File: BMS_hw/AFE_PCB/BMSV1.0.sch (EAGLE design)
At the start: 238 parts, among them IC1 MC33771BEP, IC2 SFH6156, IC3 MIC28515V1, IC4 FOD8384-COC, IC5 FOD8384-COC, IC6 FOD8384-COC, J2 NTC, Q1 IRLML5203, Q2 IRLML5203, T1 IPT020N10N3V1, T2 IPT020N10N3V1, T3 IPT020N10N3V1, T4 IPT020N10N3V1, X1 87758-2016, X2 87758-1816, X3 22-23-2041, X4 87758-2016, X5 22-23-2051

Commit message: board layout itt@1
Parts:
- removed C79, C81, C85, C87, C91: 0.047uF, ipc-7351-capacitor:CAPACITOR_0402
- removed C80, C82, C86, C88, C92: 0.47uF, ipc-7351-capacitor:CAPACITOR_0402
- removed R105: 10k, ipc-7351-resistor:RESISTOR_0402
- added C39: 0.47uF, ipc-7351-capacitor:CAPACITOR_1206
- added C40, C41: 0.047uF, ipc-7351-capacitor:CAPACITOR_0402
- added C61: 0.22uF, ipc-7351-capacitor:CAPACITOR_0402
- added C63: (no value), ipc-7351-capacitor:POLARISED_CASE_E
- added C64, C70: 47nF, ipc-7351-capacitor:CAPACITOR_1210
- added C65, C68: 47nF, ipc-7351-capacitor:CAPACITOR_0402
- added C69: 47nF, ipc-7351-capacitor:CAPACITOR_0603
- added R68, R69: 10k, ipc-7351-resistor:RESISTOR_0402
- added TP1: TPTH7035, simpa:TPTH7035
- C1: value 0.22uF -> 0.047uF; device ipc-7351-capacitor:CAPACITOR_0402 -> ipc-7351-capacitor:CAPACITOR_0603
- C10, C11, C12, C32, C33, C34, C35, C36, C37, C8: value 0.047uF -> 0.47uF; device ipc-7351-capacitor:CAPACITOR_0402 -> ipc-7351-capacitor:CAPACITOR_1206
- C13, C9: value 47nF -> 0.47uF; device ipc-7351-capacitor:CAPACITOR_0402 -> ipc-7351-capacitor:CAPACITOR_1206
- C14: value 2.2uF -> 0.47uF; device ipc-7351-capacitor:CAPACITOR_0402 -> ipc-7351-capacitor:CAPACITOR_1206
- C15: value 2.2uF -> 0.047uF
- C16: value 1uF -> 0.047uF
- C17: value 47nF -> 0.047uF
- C18, C19, C20, C21: value 0.47uF -> 0.047uF
- C2, C24, C26, C5: value 47nF -> 0.047uF; device ipc-7351-capacitor:CAPACITOR_0402 -> ipc-7351-capacitor:CAPACITOR_0603
- C22: value 47nF -> 2.2uF; device ipc-7351-capacitor:CAPACITOR_0603 -> ipc-7351-capacitor:CAPACITOR_0402
- C23: value 47nF -> .047uF; device ipc-7351-capacitor:CAPACITOR_1210 -> ipc-7351-capacitor:CAPACITOR_0402
- C25: value 47nF -> 0.047uF; device ipc-7351-capacitor:CAPACITOR_1210 -> ipc-7351-capacitor:CAPACITOR_0603
- C27, C28, C29: value 0.47uF -> 0.047uF; device ipc-7351-capacitor:CAPACITOR_0402 -> ipc-7351-capacitor:CAPACITOR_0603
- C3, C31, C4, C7: device ipc-7351-capacitor:CAPACITOR_0402 -> ipc-7351-capacitor:CAPACITOR_0603
- C30: value (none) -> 0.047uF; device ipc-7351-capacitor:CAPACITOR_0402 -> ipc-7351-capacitor:CAPACITOR_0603
- C38: value (none) -> 0.47uF; device ipc-7351-capacitor:POLARISED_CASE_E -> ipc-7351-capacitor:CAPACITOR_1206
- C6: value 6.8uF -> 0.047uF; device ipc-7351-capacitor:CAPACITOR_0402 -> ipc-7351-capacitor:CAPACITOR_0603
- C66: value .047uF -> 47nF
- C67: value 2.2uF -> 47nF
- C71: value 0.047uF -> 47nF
- C72, C74: value 0.47uF -> 47nF
- C73: value 0.047uF -> 1uF
- C75: value 0.047uF -> 6.8uF
- C76: value 0.47uF -> 2.2uF
- C77: value 0.047uF -> 2.2uF
- C78: value 0.047uF -> (none)
- D1: device ipc-7351-diode:ZENER_SOD-123 -> ipc-7351-diode:SCHOTTKY_SOD-123
- D10: value 8.2v -> (none); device ipc-7351-diode:SCHOTTKY_SOD-123 -> ipc-7351-diode:DIODE_SOD-123
- D11: value 20v -> 8.2v; device ipc-7351-diode:SCHOTTKY_SOD-123 -> ipc-7351-diode:ZENER_SOD-123
- D12: value 27v -> (none)
- D13: value 43v -> (none)
- D14: value 75v -> (none)
- D15: value 2v -> (none)
- D16: value 2v -> (none); device ipc-7351-diode:SCHOTTKY_SOD-123 -> ipc-7351-diode:ZENER_SOD-123
- D17, D18: value 2v -> SFH48225; device ipc-7351-diode:SCHOTTKY_SOD-123 -> GreenFuel:SFH48225
- D19: value (none) -> SFH48225; device ipc-7351-diode:SCHOTTKY_SOD-123 -> GreenFuel:SFH48225
- D2: value (none) -> 20v; device ipc-7351-diode:DIODE_SOD-123 -> ipc-7351-diode:SCHOTTKY_SOD-123
- D3: value SFH48225 -> 27v; device GreenFuel:SFH48225 -> ipc-7351-diode:SCHOTTKY_SOD-123
- D4: value SFH48225 -> 43v; device GreenFuel:SFH48225 -> ipc-7351-diode:SCHOTTKY_SOD-123
- D5: value SFH48225 -> 75v; device GreenFuel:SFH48225 -> ipc-7351-diode:SCHOTTKY_SOD-123
- D6: value (none) -> 2v; device ipc-7351-diode:ZENER_SOD-123 -> ipc-7351-diode:SCHOTTKY_SOD-123
- D7, D8, D9: value (none) -> 2v
- JP1: device GreenFuel:PINOLED-4 -> adafruit:PINHD-1X1CB
- JP3: device adafruit:PINHD-1X1CB -> GreenFuel:PINOLED-4
- R1: value 10 -> (none)
- R10, R9: value 180E -> (none)
- R11: value 2E2 -> 180E; device ipc-7351-resistor:RESISTOR_0402 -> ipc-7351-resistor:RESISTOR_1210
- R12: value 200k -> 180E; device ipc-7351-resistor:RESISTOR_0402 -> ipc-7351-resistor:RESISTOR_1210
- R13: value 180E -> 39E; device ipc-7351-resistor:RESISTOR_0402 -> ipc-7351-resistor:RESISTOR_1210
- R14, R6: device ipc-7351-resistor:RESISTOR_0402 -> ipc-7351-resistor:RESISTOR_1210
- R15: value 100k -> 3k
- R16, R21: value 127E -> 3k
- R2, R4: value 100 -> (none)
- R22, R23, R24, R25: value 127E -> 2k
- R26, R27, R28: value 3k -> 2k
- R3: value 127E -> (none)
- R31, R70, R72, R74, R78: value 2k -> 10k
- R32, R33, R36, R37: value 2k -> (none)
- R34: value 2k -> 0R
- R35: value 2k -> 100; device ipc-7351-resistor:RESISTOR_0402 -> ipc-7351-resistor:RESISTOR_1210
- R38, R41, R42, R8: value 10k -> (none)
- R39, R7: value LRMAP3920SUNT -> 100; device GreenFuel:LRMAP3920SUNT -> ipc-7351-resistor:RESISTOR_1210
- R40: value 10k -> 100; device ipc-7351-resistor:RESISTOR_0402 -> ipc-7351-resistor:RESISTOR_1210
- R44, R45, R50, R51, R52, R53, R54, R55: value (none) -> 3k
- R46: value 3k -> 180E; device ipc-7351-resistor:RESISTOR_0402 -> ipc-7351-resistor:RESISTOR_1210
- R47, R48, R49: value (none) -> 180E; device ipc-7351-resistor:RESISTOR_0402 -> ipc-7351-resistor:RESISTOR_1210
- R5: value 127E -> 100; device ipc-7351-resistor:RESISTOR_0402 -> ipc-7351-resistor:RESISTOR_1210
- R56, R57, R58: value (none) -> 2k
- R59, R60, R61, R62, R63: value 10k -> 2k
- R66: value 10k -> 10
- R71, R73, R77: value 3k -> 10k
- R75: value 100 -> 10k
- R76: value 180E -> 10k
- R79, R83, R85: value 3k -> 127E
- R80, R86: value 2k -> 127E
- R81: value 100 -> LRMAP3920SUNT; device ipc-7351-resistor:RESISTOR_0402 -> GreenFuel:LRMAP3920SUNT
- R82, R88: value 180E -> 127E
- R84: value 2k -> LRMAP3920SUNT; device ipc-7351-resistor:RESISTOR_0402 -> GreenFuel:LRMAP3920SUNT
- R87: value 100 -> 127E
- R89: value 180E -> 100k
- R90: value 2k -> 200k
- R91: value 3k -> 2E2
- X1: value 87758-2016 -> 87758-1816; device con-molex:87758-2016 -> con-molex:87758-1816
- X2: value 87758-1816 -> 87758-2016; device con-molex:87758-1816 -> con-molex:87758-2016
- X3: value 22-23-2041 -> 87758-2016; device GreenFuel:22-23-2041 -> con-molex:87758-2016
- X4: value 87758-2016 -> 22-23-2051; device con-molex:87758-2016 -> GreenFuel:22-23-2051
- X5: value 22-23-2051 -> 22-23-2041; device GreenFuel:22-23-2051 -> GreenFuel:22-23-2041
- renumbered C100 to C62, C101 to C60, C102 to C48, C103 to C49, C104 to C50, C105 to C52, C106 to C53, C107 to C51, C108 to C54, C83 to C43, C84 to C42, C89 to C45, C90 to C44, C93 to C46, C94 to C47, C95 to C59, C96 to C55, C97 to C56, C98 to C57, C99 to C58, J2 to J1
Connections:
- removed net 15V_AUX: IC4.VDD, IC5.VDD, IC6.VDD, X4-17.S
- removed net C_FET: X4-9.S
- removed net D_FET: X4-19.S
- removed net N$26: C66.1, IC1.VANA
- removed net N$42: C74.1, R71.2, R72.1
- removed net N$44: C80.1, R77.2, R78.1
- removed net N$45: C82.1, R79.2, R80.1
- removed net N$47: C88.1, R85.2, R86.1
- removed net N$63: CELL1-.S, R53.1
- removed net VBATT-: R42.1
- removed net VCC: C22.1, C23.1, L1.2, R22.1
- new net +15V: C69.1, C70.1, IC4.VDD, IC5.VDD, IC6.VDD, L1.2, R85.1, X2-17.S
- new net BGND: CELL1-.S, R34.1, R38.1, R81.4, R84.4
- new net GATE: D10.K, D11.K, R93.1, R94.2, T3.G, T4.G
- new net N$10: C38.1, R54.2, R62.1
- new net N$16: C37.1, R53.2, R60.1
- new net N$23: C36.1, R52.2, R59.1
- new net PCHG_GATE: IC6.ANODE, X2-4.S
- new net VANA: C23.1, IC1.VANA
- net !MCLR: now also X2-10.S, X4-5.S; no longer X4-10.S, X5-5.S
- net 3.3V: now also JP3.3, R101.2, X2-12.S, X3-16.S, X4-4.S; no longer JP1.3, R59.2, X1-16.S, X4-12.S, X5-4.S
- net AGND: now also X1-1.S; no longer X2-1.S
- net BST: now also C65.1; no longer C24.1
- net CANH: now also D15.K, X5-4.S; no longer D19.K, X3-4.S
- net CANL: now also D14.K, X5-3.S; no longer D9.K, X3-3.S
- net CB_1: now also R49.2; no longer R89.2
- net CB_10/9_C: now also C7.1, D2.A, R10.1, R17.1; no longer C12.1, D11.A, R19.1, R58.1
- net CB_11: now also R6.2; no longer R4.2
- net CB_12: now also D4.A, R11.2; no longer D13.A, R9.2
- net CB_12/11_C: now also C6.1, R16.1, R9.2; no longer C11.1, R18.1, R56.2
- net CB_13: now also R7.2; no longer R6.2
- net CB_13/12_C: now also C1.1, R1.2, R11.1, R20.1, R7.1; no longer C3.1, R27.1, R44.2, R6.1, R9.1
- net CB_13/12_C1: now also C4.1, R21.1, R4.2, R6.1; no longer C8.1, R28.1, R4.1, R45.2
- net CB_13/12_C2: now also C2.1, R12.1, R18.1, R2.2, R5.1; no longer C4.1, R10.1, R2.1, R20.1, R47.2
- net CB_13/12_C6: now also C26.1, R36.2, R39.1, R46.1, R51.1; no longer C73.1, R49.2, R71.1, R75.1, R76.1
- net CB_13/12_C7: now also C24.1, R32.2, R35.1, R47.1, R52.1; no longer C79.1, R51.2, R77.1, R81.1, R82.1
- net CB_13/12_C8: now also C28.1, R37.2, R40.1, R48.1, R55.1; no longer C85.1, R52.2, R83.1, R87.1, R88.1
- net CB_14: now also D3.A; no longer D12.A
- net CB_14/13_C: now also C5.1, R15.1, R8.2; no longer C10.1, R17.1, R57.2
- net CB_2: now also R48.2; no longer R88.2
- net CB_2/1_C: now also C31.1, R41.2, R54.1; no longer C87.1, R55.2, R85.1
- net CB_3: now also R40.2; no longer R87.2
- net CB_4: now also R47.2; no longer R82.2
- net CB_4/3_C: now also C30.1, R43.2, R53.1; no longer C81.1, R54.2, R79.1
- net CB_5: now also R35.2; no longer R81.2
- net CB_6: now also R46.2; no longer R76.2
- net CB_6/5_C: now also C25.1, R33.2, R44.1; no longer C75.1, R50.2, R73.1
- net CB_7: now also R39.2; no longer R75.2
- net CB_8: now also R12.2; no longer R10.2
- net CB_8/7_C: now also C29.1, D1.A, R42.2, R50.1; no longer C71.1, D10.A, R46.1, R48.2
- net CB_9: now also R5.2; no longer R2.2
- net CELL1-: now also C27.1, R38.2, R45.1, R49.1, R98.1; no longer C91.1, R53.2, R89.1, R91.1
- net CELL14+: now also C3.1, R19.1, R3.2, R66.1; no longer C7.1, R1.1, R26.1, R43.2
- net CHG_FET: now also IC5.VO, Q1.S; no longer IC4.ANODE
- net CHG_GATE: now also IC5.ANODE, X2-9.S; no longer D1.K, D2.K, IC6.VO, Q1.S, R30.2, R38.1, T1.G, T2.G
- net CT_1: now also R62.2; no longer R86.2
- net CT_10: now also C18.2, C19.1, R26.2; no longer C34.2, C35.1, R35.2
- net CT_11: now also C17.2, C18.1, R25.2; no longer C33.2, C34.1, R34.2
- net CT_12: now also C16.2, C17.1, R24.2; no longer C32.2, C33.1, R33.2
- net CT_13: now also C15.2, C16.1, R23.2; no longer C31.2, C32.1, R32.2
- net CT_14: now also C15.1, R22.2; no longer C31.1, R31.2
- net CT_2: now also R61.2; no longer R84.2
- net CT_3: now also R60.2; no longer R80.2
- net CT_4: now also R59.2; no longer R78.2
- net CT_5: now also C41.2, R58.2; no longer C77.2, R74.2
- net CT_6: now also C40.2, C41.1, R57.2; no longer C77.1, C78.2, R72.2
- net CT_7: now also C21.2, C40.1, R56.2; no longer C37.2, C78.1, R70.2
- net CT_8: now also C20.2, C21.1, R28.2; no longer C36.2, C37.1, R37.2
- net CT_9: now also C19.2, C20.1, R27.2; no longer C35.2, C36.1, R36.2
- net CT_REF: now also R63.2; no longer R90.2
- net C_HIGH(VC14): now also X1-18.S; no longer X2-18.S
- net DSG_FET: now also IC4.VO, R92.2, T1.G, T2.G; no longer IC6.ANODE
- net DSG_GATE: now also IC4.ANODE, X2-19.S; no longer IC4.VO, R29.2, T3.G, T4.G
- net FAULT: now also X2-5.S; no longer X4-5.S
- net FB: now also C66.2, R85.2, R86.1; no longer C17.2, R22.2, R23.1
- net GND: now also C24.2, C30.2, C31.2, C32.2, C33.2, C34.2, C35.2, C36.2, C37.2, C38.2, C39.2, C6.2, C61.2, C63.-, C64.2, C68.2, C69.2, C70.2, C77.2, C78.1, D15.A, D16.A, D5.A, D7.K, D9.K, JP3.4, R100.2, R102.2, R103.2, R104.2, R30.2, R34.2, R86.2, R89.2, R95.2, R96.2, R97.2, X1-11.S, X2-1.S, X2-15.S, X2-18.S, X2-2.S, X2-20.S, X2-3.S, X2-6.S, X2-7.S, X2-8.S, X3-1.S, X3-10.S, X3-14.S, X3-18.S, X3-2.S, X3-20.S, X3-3.S, X3-7.S, X3-8.S; no longer C15.2, C16.2, C18.2, C19.2, C20.2, C21.2, C30.1, C38.-, C66.2, C75.2, C79.2, C80.2, C81.2, C82.2, C85.2, C86.2, C87.2, C88.2, C91.2, C92.2, D16.K, D18.K, D19.A, D6.A, D9.A, JP1.4, R15.2, R23.2, R39.4, R40.2, R41.2, R60.2, R61.2, R62.2, R65.2, R67.2, R7.4, R8.2, X1-1.S, X1-10.S, X1-14.S, X1-18.S, X1-2.S, X1-20.S, X1-3.S, X1-7.S, X1-8.S, X2-11.S, X4-15.S, X4-18.S, X4-2.S, X4-20.S, X4-3.S, X4-6.S, X4-7.S, X4-8.S, X5-1.S
- net GPIO0: now also R72.1; no longer R99.1
- net GPIO1: now also R73.1; no longer R100.1
- net GPIO2: now also R74.1; no longer R101.1
- net GPIO3: now also R75.1; no longer R102.1
- net GPIO4: now also R76.1; no longer R103.1
- net GPIO5: now also R77.1; no longer R104.1
- net GPIO6: now also R78.1; no longer R105.1
- net ILIM: now also R80.1, R82.1; no longer R16.1, R24.1
- net INTL_IN2: now also D12.A, X5-1.S; no longer D7.A, X3-1.S
- net INTL_OUT1: now also JP2.1, X5-2.S; no longer JP3.1, X3-2.S
- net ISENSE+: now also C71.1, C75.1, R87.2; no longer C13.1, C6.1, R5.2
- net ISENSE-: now also C72.1, C75.2, R88.2; no longer C2.1, C6.2, R3.2
- net ISP: now also X2-11.S; no longer X4-11.S
- net KEY-IN: now also D12.K, D13.K, R99.1; no longer D7.K, D8.K, R63.1
- net N$1: now also C12.1, R19.2, R22.1; no longer C27.1, R26.2, R31.1
- net N$11: now also D6.A, D7.A; no longer D17.A, D18.A
- net N$17: now also R89.1, R90.1; no longer R12.1, R15.1
- net N$18: now also C73.1; no longer C16.1
- net N$19: now also D10.A, R93.2; no longer D2.A, R38.2
- net N$2: now also C11.1, R18.2, R28.1; no longer C21.1, R20.2, R37.1
- net N$20: now also IC5.CATHODE, R96.1; no longer IC4.CATHODE, R8.1
- net N$21: now also C74.1, R79.2; no longer C26.1, R25.2
- net N$24: now also C66.1, R83.2; no longer C17.1, R21.2
- net N$25: now also IC4.CATHODE, R95.1; no longer IC6.CATHODE, R40.1
- net N$27: now also IC6.CATHODE, R97.1; no longer IC5.CATHODE, R41.1
- net N$28: now also R98.2; no longer R42.2
- net N$29: now also C63.+, C64.1, R3.1, R79.1; no longer C25.1, C38.+, R25.1, R43.1
- net N$3: now also D8.A, D9.A; no longer D15.A, D16.A
- net N$30: now also R31.1; no longer R64.1
- net N$31: now also R31.2; no longer R64.2
- net N$33: now also R36.1; no longer R49.1
- net N$34: now also R29.1; no longer R66.1
- net N$35: now also R33.1; no longer R50.1
- net N$37: now also R1.1; no longer R44.1
- net N$38: now also C35.1, R51.2, R57.1; no longer IC5.VO
- net N$39: now also R4.1; no longer R45.1
- net N$4: now also C14.1, R21.2, R26.1; no longer C29.1, R28.2, R35.1
- net N$40: now also R2.1; no longer R47.1
- net N$41: now also C34.1, R50.2, R56.1; no longer C72.1, R46.2, R70.1
- net N$43: now also R42.1; no longer R48.1
- net N$46: now also C39.1, R55.2, R61.1; no longer C86.1, R83.2, R84.1
- net N$48: now also C33.1, R45.2, R63.1; no longer C92.1, R90.1, R91.2
- net N$49: now also R64.1, R72.2; no longer R92.1, R99.2
- net N$5: now also C13.1, R20.2, R24.1; no longer C28.1, R27.2, R33.1
- net N$50: now also R65.1, R73.2; no longer R100.2, R93.1
- net N$51: now also R67.1, R74.2; no longer R101.2, R94.1
- net N$52: now also R68.1, R75.2; no longer R102.2, R95.1
- net N$53: now also R69.1, R76.2; no longer R103.2, R96.1
- net N$54: now also R70.1, R77.2; no longer R104.2, R97.1
- net N$55: now also R71.1, R78.2; no longer R105.2, R98.1
- net N$58: now also R32.1; no longer R51.1
- net N$59: now also R43.1; no longer R54.1
- net N$6: now also C8.1, R15.2, R23.1; no longer C18.1, R17.2, R32.1
- net N$60: now also R37.1; no longer R52.1
- net N$62: now also R41.1; no longer R55.1
- net N$64: now also R9.1; no longer R56.1
- net N$65: now also R8.1; no longer R57.1
- net N$66: now also R10.2; no longer R58.2
- net N$68: now also C67.1, D6.K, R81.5, R84.5, R87.1; no longer C9.1, D17.K, R39.5, R5.1, R7.5
- net N$7: now also C10.1, R17.2, R27.1; no longer C20.1, R19.2, R36.1
- net N$70: now also C68.1, D8.K, R81.2, R84.2, R88.1; no longer C5.1, D15.K, R3.1, R39.2, R7.2
- net N$71: now also R101.1; no longer R59.1
- net N$72: now also D19.C, R104.1; no longer D4.C, R62.1
- net N$73: now also D18.C, R103.1; no longer D5.C, R60.1
- net N$74: now also D17.C, R102.1; no longer D3.C, R61.1
- net N$78: now also D13.A, JP1.1; no longer D8.A, JP2.1
- net N$8: now also C32.1, R44.2, R58.1; no longer C76.1, R73.2, R74.1
- net N$9: now also C9.1, R16.2, R25.1; no longer C19.1, R18.2, R34.1
- net OLED_SCL: now also JP3.2, X3-6.S; no longer JP1.2, X1-6.S
- net OLED_SDA: now also JP3.1, X3-4.S; no longer JP1.1, X1-4.S
- net PCHG_FET: now also IC6.VO; no longer IC5.ANODE, X4-4.S
- net PVDD: now also C77.1, R91.1; no longer C15.1, R11.1
- net RDTX_OUT+: now also X3-5.S; no longer X1-5.S
- net RDTX_OUT-: now also X3-9.S; no longer X1-9.S
- net RESET: now also R30.1; no longer R67.1
- net RX_O: now also X2-14.S, X4-2.S; no longer X4-14.S, X5-2.S
- net S-LED_1: now also X3-11.S; no longer X1-11.S
- net S-LED_2: now also X3-13.S; no longer X1-13.S
- net S-LED_3: now also D17.A, X3-15.S; no longer D3.A, X1-15.S
- net S-LED_4: now also D18.A, X3-17.S; no longer D5.A, X1-17.S
- net S-LED_5: now also D19.A, X3-19.S; no longer D4.A, X1-19.S
- net SW: now also C65.2, R80.2, R82.2, R83.1; no longer C24.2, R16.2, R21.1, R24.2
- net T: now also X1-10.S; no longer X2-10.S
- net TX_O: now also X2-16.S, X4-3.S; no longer X4-16.S, X5-3.S
- net T_SUPPLY: now also X1-2.S; no longer X2-2.S
- net V+: now also D11.A, R94.1, T3.S, T3.S1, T3.S2, T3.S3, T3.S4, T3.S5, T3.S6, T4.S, T4.S1, T4.S2, T4.S3, T4.S4, T4.S5, T4.S6; no longer D1.A, R30.1, T1.S, T1.S1, T1.S2, T1.S3, T1.S4, T1.S5, T1.S6, T2.S, T2.S1, T2.S2, T2.S3, T2.S4, T2.S5, T2.S6
- net V-: now also R81.1, R84.1, R92.1, T1.S, T1.S1, T1.S2, T1.S3, T1.S4, T1.S5, T1.S6, T2.S, T2.S1, T2.S2, T2.S3, T2.S4, T2.S5, T2.S6; no longer R29.1, R39.1, R7.1, T3.S, T3.S1, T3.S2, T3.S3, T3.S4, T3.S5, T3.S6, T4.S, T4.S1, T4.S2, T4.S3, T4.S4, T4.S5, T4.S6
- net VC1: now also X1-3.S; no longer X2-3.S
- net VC10: now also X1-16.S; no longer X2-16.S
- net VC11: now also X1-8.S; no longer X2-8.S
- net VC12: now also X1-17.S; no longer X2-17.S
- net VC13: now also X1-9.S; no longer X2-9.S
- net VC2: now also X1-12.S; no longer X2-12.S
- net VC3: now also X1-4.S; no longer X2-4.S
- net VC4: now also X1-13.S; no longer X2-13.S
- net VC5: now also X1-5.S; no longer X2-5.S
- net VC6: now also X1-14.S; no longer X2-14.S
- net VC7: now also X1-6.S; no longer X2-6.S
- net VC8: now also X1-15.S; no longer X2-15.S
- net VC9: now also X1-7.S; no longer X2-7.S
- net VCOM: now also C22.1, R29.2, R64.2, R65.2, R67.2, R68.2, R69.2, R70.2, R71.2; no longer C67.1, R66.2, R92.2, R93.2, R94.2, R95.2, R96.2, R97.2, R98.2
- net VDD: now also C76.1, R91.2, X2-13.S, X3-12.S; no longer C14.1, R11.2, X1-12.S, X4-13.S
- net VIN: now also R90.2; no longer R12.2
- net VPWR: now also C61.1, D1.K, D2.K, D3.K, D4.K, D5.K, R66.2; no longer C1.1, D10.K, D11.K, D12.K, D13.K, D14.K, R1.2
- net WAKE: now also C78.2, D16.K, R100.1, R99.2; no longer C30.2, D6.K, R63.2, R65.1

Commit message: afe board and schematic files are updatd !
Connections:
- net C_HIGH(VC14) renamed N$33
- net N$64 renamed CELL11+
- net N$65 renamed CELL13
- net VC10 renamed N$26
- removed net AGND: X1-1.S
- removed net N$33 (its old number): CELL6+.S, R36.1
- removed net N$35: CELL5+.S, R33.1
- removed net N$37: CELL12+.S, R1.1
- removed net N$39: CELL10+.S, R4.1
- removed net N$40: CELL8+.S, R2.1
- removed net N$43: CELL7+.S, R42.1
- removed net N$58: CELL4+.S, R32.1
- removed net N$59: CELL3+.S, R43.1
- removed net N$60: CELL2+.S, R37.1
- removed net N$62: CELL1+.S, R41.1
- removed net N$66: CELL9+.S, R10.2
- removed net T: X1-10.S
- removed net T_SUPPLY: X1-2.S
- removed net VC1: X1-3.S
- removed net VC11: X1-8.S
- removed net VC12: X1-17.S
- removed net VC13: X1-9.S
- removed net VC2: X1-12.S
- removed net VC3: X1-4.S
- removed net VC4: X1-13.S
- removed net VC5: X1-5.S
- removed net VC6: X1-14.S
- removed net VC7: X1-6.S
- removed net VC8: X1-15.S
- removed net VC9: X1-7.S
- new net CELL1+: CELL1+.S, R41.1, X1-2.S, X1-9.S
- new net CELL10+: CELL10+.S, R4.1, X1-10.S
- new net CELL12+: CELL12+.S, R1.1, X1-12.S
- new net CELL2+: CELL2+.S, R37.1, X1-5.S
- new net CELL3+: CELL3+.S, R43.1, X1-11.S
- new net CELL4+: CELL4+.S, R32.1, X1-3.S, X1-4.S
- new net CELL5+: CELL5+.S, R33.1, X1-13.S
- new net CELL6+: CELL6+.S, R36.1, X1-1.S, X1-6.S
- new net CELL7+: CELL7+.S, R42.1, X1-15.S
- new net CELL8+: CELL8+.S, R2.1, X1-8.S
- new net CELL9+: CELL9+.S, R10.2, X1-17.S
- net BGND: now also X1-7.S
- net CELL14+: now also CELL14+.S, R3.1, X1-14.S
- net GND: no longer X1-11.S
- net N$29: no longer CELL14+.S, R3.1

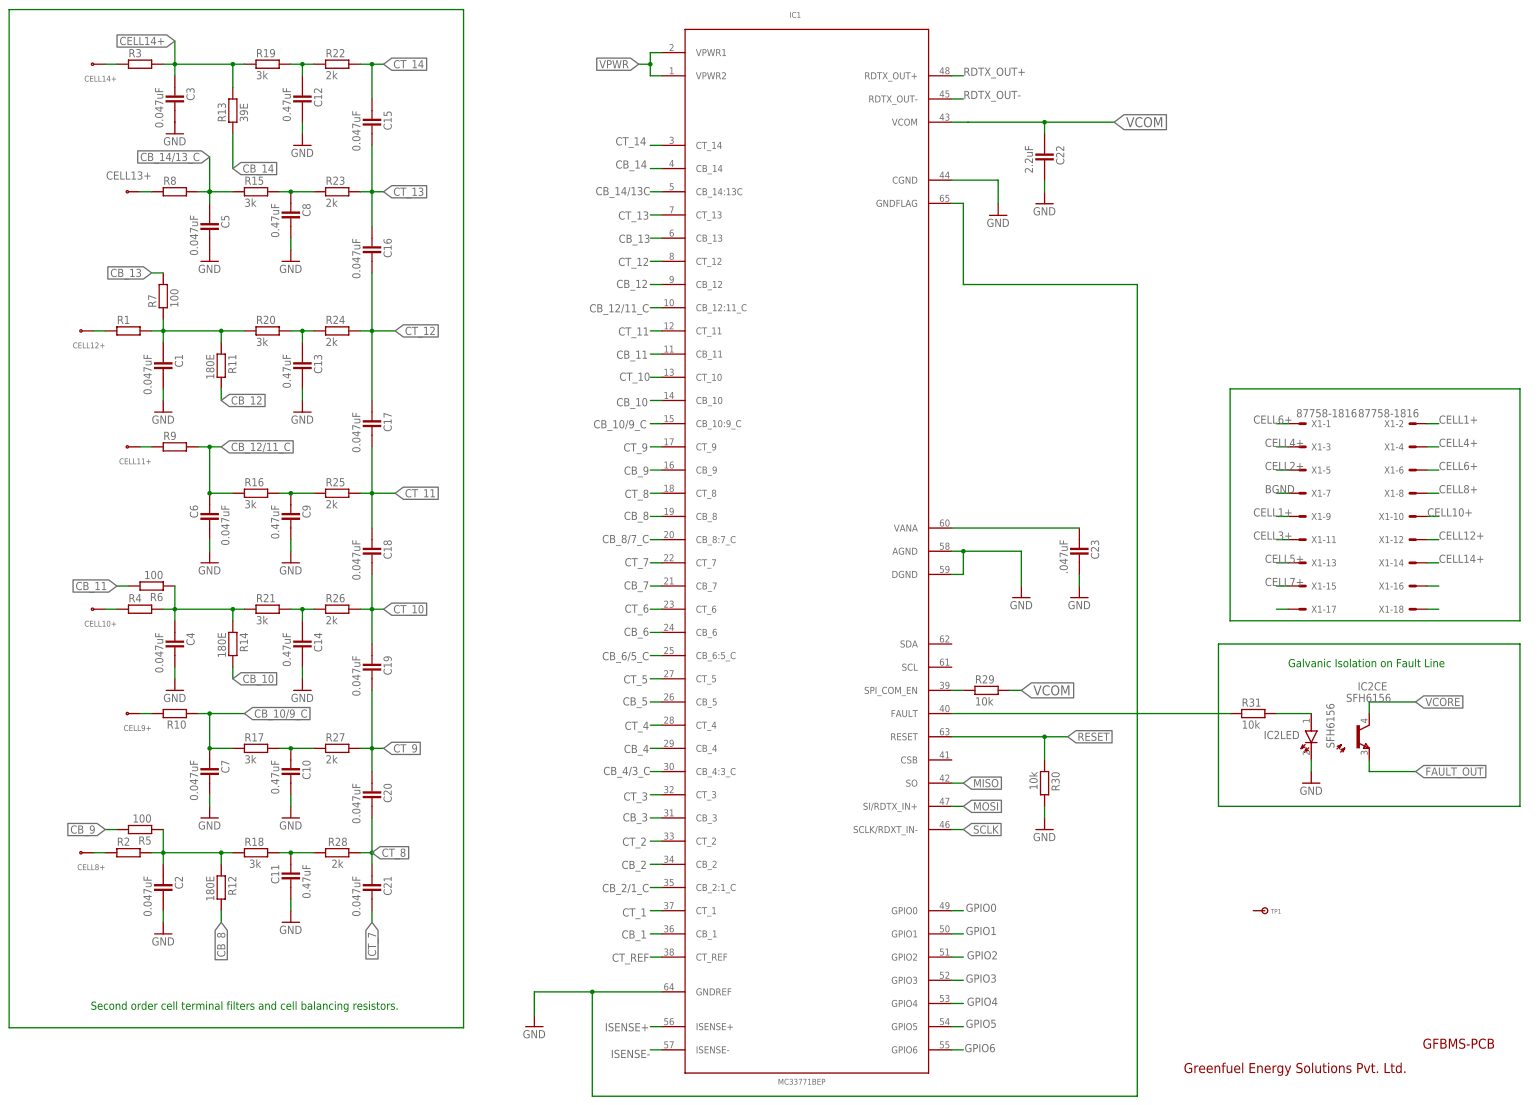
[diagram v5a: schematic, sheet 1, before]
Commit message: brd, lyout changed
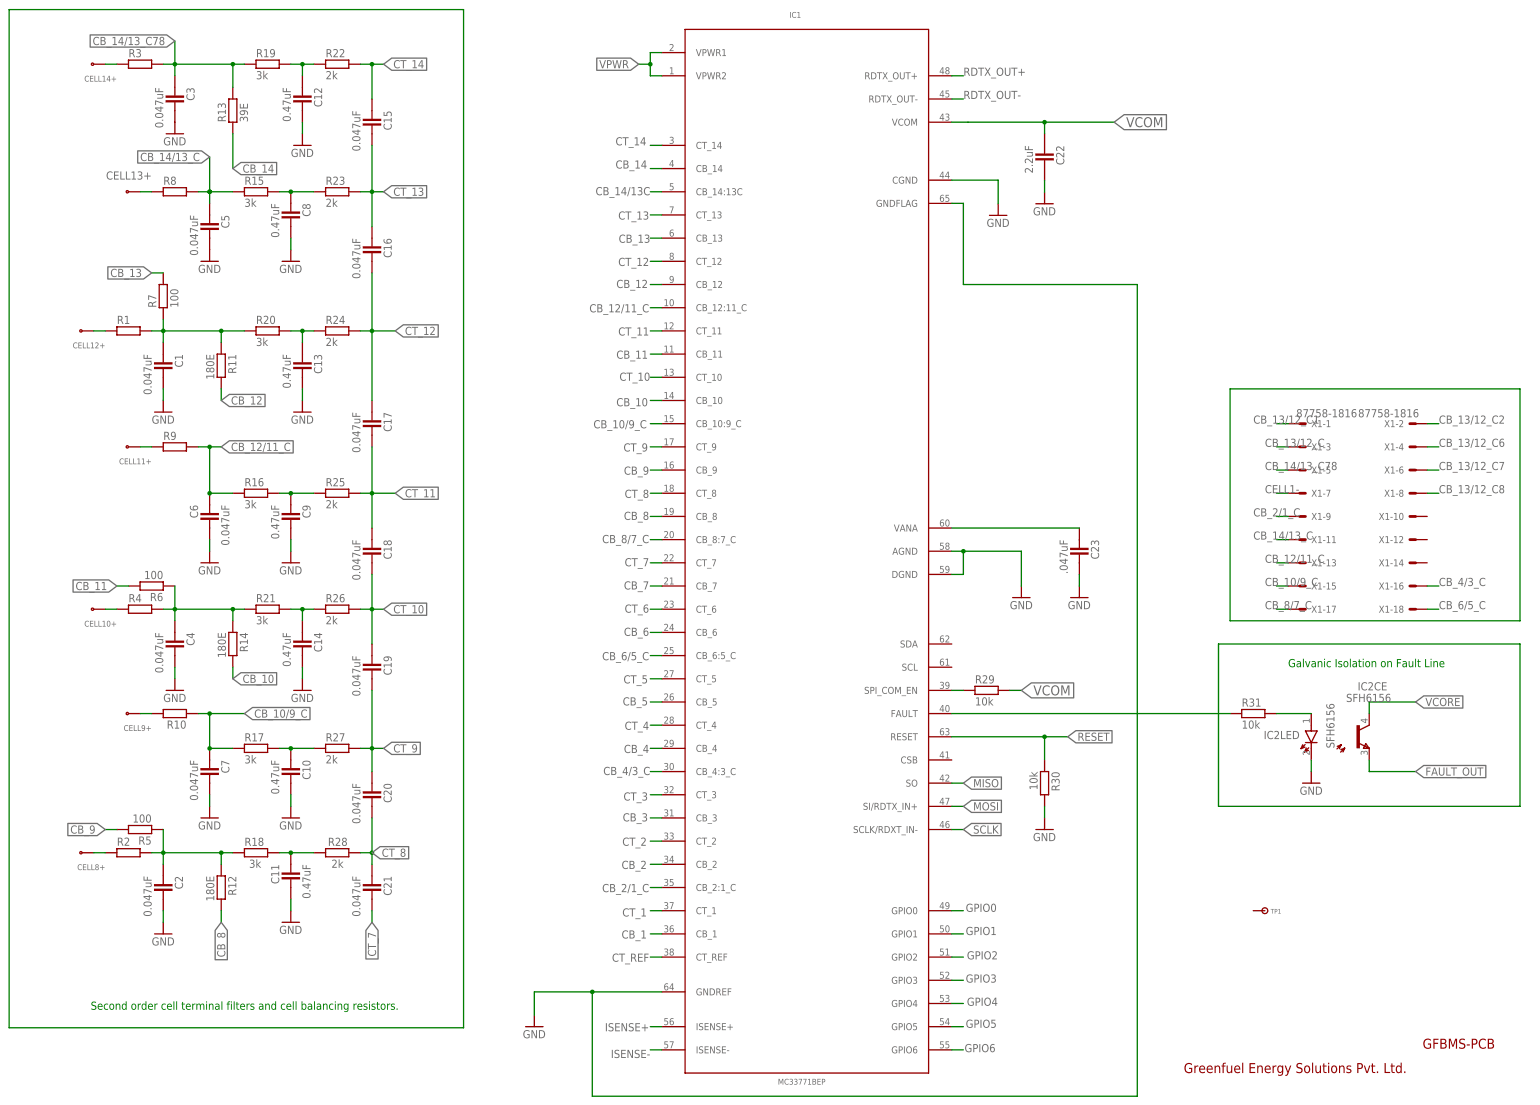
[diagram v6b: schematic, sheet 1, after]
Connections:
- net CELL13 renamed CELL13+
- removed net N$26: X1-16.S
- removed net N$33: X1-18.S
- new net CB_14/13_C78: C3.1, R13.2, R19.1, R3.2, X1-5.S
- net BGND: now also R98.1; no longer X1-7.S
- net CB_10/9_C: now also X1-15.S
- net CB_12/11_C: now also X1-13.S
- net CB_13/12_C: now also X1-3.S
- net CB_13/12_C1: now also X1-1.S
- net CB_13/12_C2: now also X1-2.S
- net CB_13/12_C6: now also X1-4.S
- net CB_13/12_C7: now also X1-6.S
- net CB_13/12_C8: now also X1-8.S
- net CB_14/13_C: now also X1-11.S
- net CB_2/1_C: now also X1-9.S
- net CB_4/3_C: now also X1-16.S
- net CB_6/5_C: now also X1-18.S
- net CB_8/7_C: now also X1-17.S
- net CELL1+: no longer X1-2.S, X1-9.S
- net CELL1-: now also X1-7.S; no longer R98.1
- net CELL10+: no longer X1-10.S
- net CELL12+: no longer X1-12.S
- net CELL14+: no longer C3.1, R13.2, R19.1, R3.2, X1-14.S
- net CELL2+: no longer X1-5.S
- net CELL3+: no longer X1-11.S
- net CELL4+: no longer X1-3.S, X1-4.S
- net CELL5+: no longer X1-13.S
- net CELL6+: no longer X1-1.S, X1-6.S
- net CELL7+: no longer X1-15.S
- net CELL8+: no longer X1-8.S
- net CELL9+: no longer X1-17.S

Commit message: brd : layout :sch update@4
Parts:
- removed R95, R97: 10k, ipc-7351-resistor:RESISTOR_0402
- removed X1: 87758-1816, con-molex:87758-1816
- added C79: 0.1uF, ipc-7351-capacitor:CAPACITOR_0603
- added D20: 8.2V, ipc-7351-diode:ZENER_SOD-123
- added JP5: (no value), GreenFuel:PINHD-1X15
- added R105, R106: 127E, ipc-7351-resistor:RESISTOR_0603
- C22, C67, C68: device ipc-7351-capacitor:CAPACITOR_0402 -> ipc-7351-capacitor:CAPACITOR_0603
- C61: device ipc-7351-capacitor:CAPACITOR_0402 -> ipc-7351-capacitor:CAPACITOR_0805
- D1: value 8.2v -> 43V; device ipc-7351-diode:SCHOTTKY_SOD-123 -> ipc-7351-diode:ZENER_SOD-323
- D2: value 20v -> 27V; device ipc-7351-diode:SCHOTTKY_SOD-123 -> ipc-7351-diode:ZENER_SOD-123
- D3: value 27v -> 8.2V; device ipc-7351-diode:SCHOTTKY_SOD-123 -> ipc-7351-diode:ZENER_SOD-123
- D4: value 43v -> 20V; device ipc-7351-diode:SCHOTTKY_SOD-123 -> ipc-7351-diode:ZENER_SOD-123
- D5: value 75v -> 75V; device ipc-7351-diode:SCHOTTKY_SOD-123 -> ipc-7351-diode:ZENER_SOD-123
- D6, D7, D8, D9: device ipc-7351-diode:SCHOTTKY_SOD-123 -> ipc-7351-diode:ZENER_SOD-123
- R87, R88: device ipc-7351-resistor:RESISTOR_0402 -> ipc-7351-resistor:RESISTOR_0603
- R96: value 10k -> 127E; device ipc-7351-resistor:RESISTOR_0402 -> ipc-7351-resistor:RESISTOR_0603
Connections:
- removed net N$25: IC4.CATHODE, R95.1
- removed net N$27: IC6.CATHODE, R97.1
- new net CB_5/4_C: JP5.4
- new net CB_7/6_C: JP5.6
- new net N$26: D20.A, D3.K
- new net N$33: IC5.ANODE, R96.2
- new net N$35: IC6.ANODE, R106.2
- net CB_10/9_C: now also JP5.14; no longer X1-15.S
- net CB_12/11_C: now also JP5.12; no longer X1-13.S
- net CB_13/12_C: now also JP5.11; no longer X1-3.S
- net CB_13/12_C1: now also JP5.13; no longer X1-1.S
- net CB_13/12_C2: now also JP5.15, JP5.9; no longer X1-2.S
- net CB_13/12_C6: no longer X1-4.S
- net CB_13/12_C7: no longer X1-6.S
- net CB_13/12_C8: no longer X1-8.S
- net CB_14/13_C: now also JP5.10; no longer X1-11.S
- net CB_14/13_C78: no longer X1-5.S
- net CB_2/1_C: now also JP5.2; no longer X1-9.S
- net CB_4/3_C: now also JP5.3; no longer X1-16.S
- net CB_6/5_C: now also JP5.5; no longer X1-18.S
- net CB_8/7_C: now also JP5.7, JP5.8; no longer X1-17.S
- net CELL1-: now also JP5.1; no longer X1-7.S
- net CHG_GATE: now also R96.1; no longer IC5.ANODE
- net DSG_GATE: now also R105.1; no longer IC4.ANODE
- net GND: now also C79.2, IC4.CATHODE, IC5.CATHODE, IC6.CATHODE; no longer R95.2, R96.2, R97.2
- net N$20: now also IC4.ANODE, R105.2; no longer IC5.CATHODE, R96.1
- net PCHG_GATE: now also R106.1; no longer IC6.ANODE
- net VCOM: now also C79.1
- net VPWR: now also D20.K; no longer D3.K
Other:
- moved on the sheet: R96

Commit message: itt@5
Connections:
- net CB_13/12_C8 renamed CB_3/2_C
- removed net CB_13/12_C1: C4.1, JP5.13, R14.1, R21.1, R4.2, R6.1
- removed net CB_13/12_C6: C26.1, R36.2, R39.1, R46.1, R51.1
- removed net CB_13/12_C7: C24.1, R32.2, R35.1, R47.1, R52.1
- removed net CB_14/13_C78: C3.1, R13.2, R19.1, R3.2
- new net CB_11/10_C: C4.1, JP5.10, R14.1, R21.1, R4.2, R6.1
- new net CB_14+/14_C: C3.1, JP5.14, R13.2, R19.1, R3.2
- new net CB_9/8_C: C2.1, JP5.8, R12.1, R18.1, R2.2, R5.1
- net CB_10/9_C: now also JP5.9; no longer JP5.14
- net CB_12/11_C: now also JP5.11; no longer JP5.12
- net CB_13/12_C: now also JP5.12; no longer JP5.11
- net CB_13/12_C2: no longer C2.1, JP5.9, R12.1, R18.1, R2.2, R5.1
- net CB_14/13_C: now also JP5.13; no longer JP5.10
- net CB_5/4_C: now also C24.1, R32.2, R35.1, R47.1, R52.1
- net CB_7/6_C: now also C26.1, R36.2, R39.1, R46.1, R51.1
- net CB_8/7_C: no longer JP5.8
